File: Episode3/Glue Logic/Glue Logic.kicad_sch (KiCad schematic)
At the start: 5 parts, among them J1 5V DC

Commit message: Pushing back everything, due to PC reinstall.
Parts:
- removed A1: Arduino Mega 2560 R3, symbol 6309 v2.0:Arduino_Mega2560_R3_Shield
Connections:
- no-connect marks 38 -> 12
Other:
- sheet Logic Devices renamed Glue Logic
- sheet CPU, Reset & Buffers ports: added none; removed ~{RST_{trigger}}
- sheet Glue Logic: file PLD.kicad_sch -> Glue.kicad_sch
- sheet Glue Logic ports: added ~{CPU_{halt}}, ~{MRDY}, ~{RD}, ~{WR}; removed CLK_{in}, FW_{update}, RTC_{as}, RTC_{ds}, SPD_{led}^{G}, SPD_{led}^{R}, ~{ACIA1_{cs}}, ~{ACIA2_{cs}}, ~{CART_{cs}}, ~{CART_{detect}}, ~{CONST}, ~{FIRQ_{reg}}, ~{HALT_{bus}}, ~{HALT}, ~{IRQ_{reg}}, ~{RTC_{cs}}, ~{STAT_{reg}}, ~{UB_RD}, ~{UB_WR}

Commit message: Tied up a few loose ends in the PLD page.
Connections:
- no-connect marks 12 -> 38
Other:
- sheet Glue Logic ports: added PSG_{clk}, RTC_{as}, RTC_{ds}, SPD_{led}^{R}, WS[0..2], ~{ACIA_{cs}}, ~{CF_{cs}}, ~{CONST}, ~{FIRQ_{vec}}, ~{IRQ_{vec}}, ~{PAGE}, ~{PHY1_{reg}}, ~{PHY2_{reg}}, ~{PSG_{dtack}}, ~{REG}, ~{RTC_{cs}}, ~{STAT1_{reg}}, ~{STAT2_{reg}}, ~{TBC1}, ~{TBC2}, ~{TIMER_{cs}}, ~{VDP_{wait}}, ~{WAIT1}, ~{WAIT2}, ~{WAIT3}; removed none

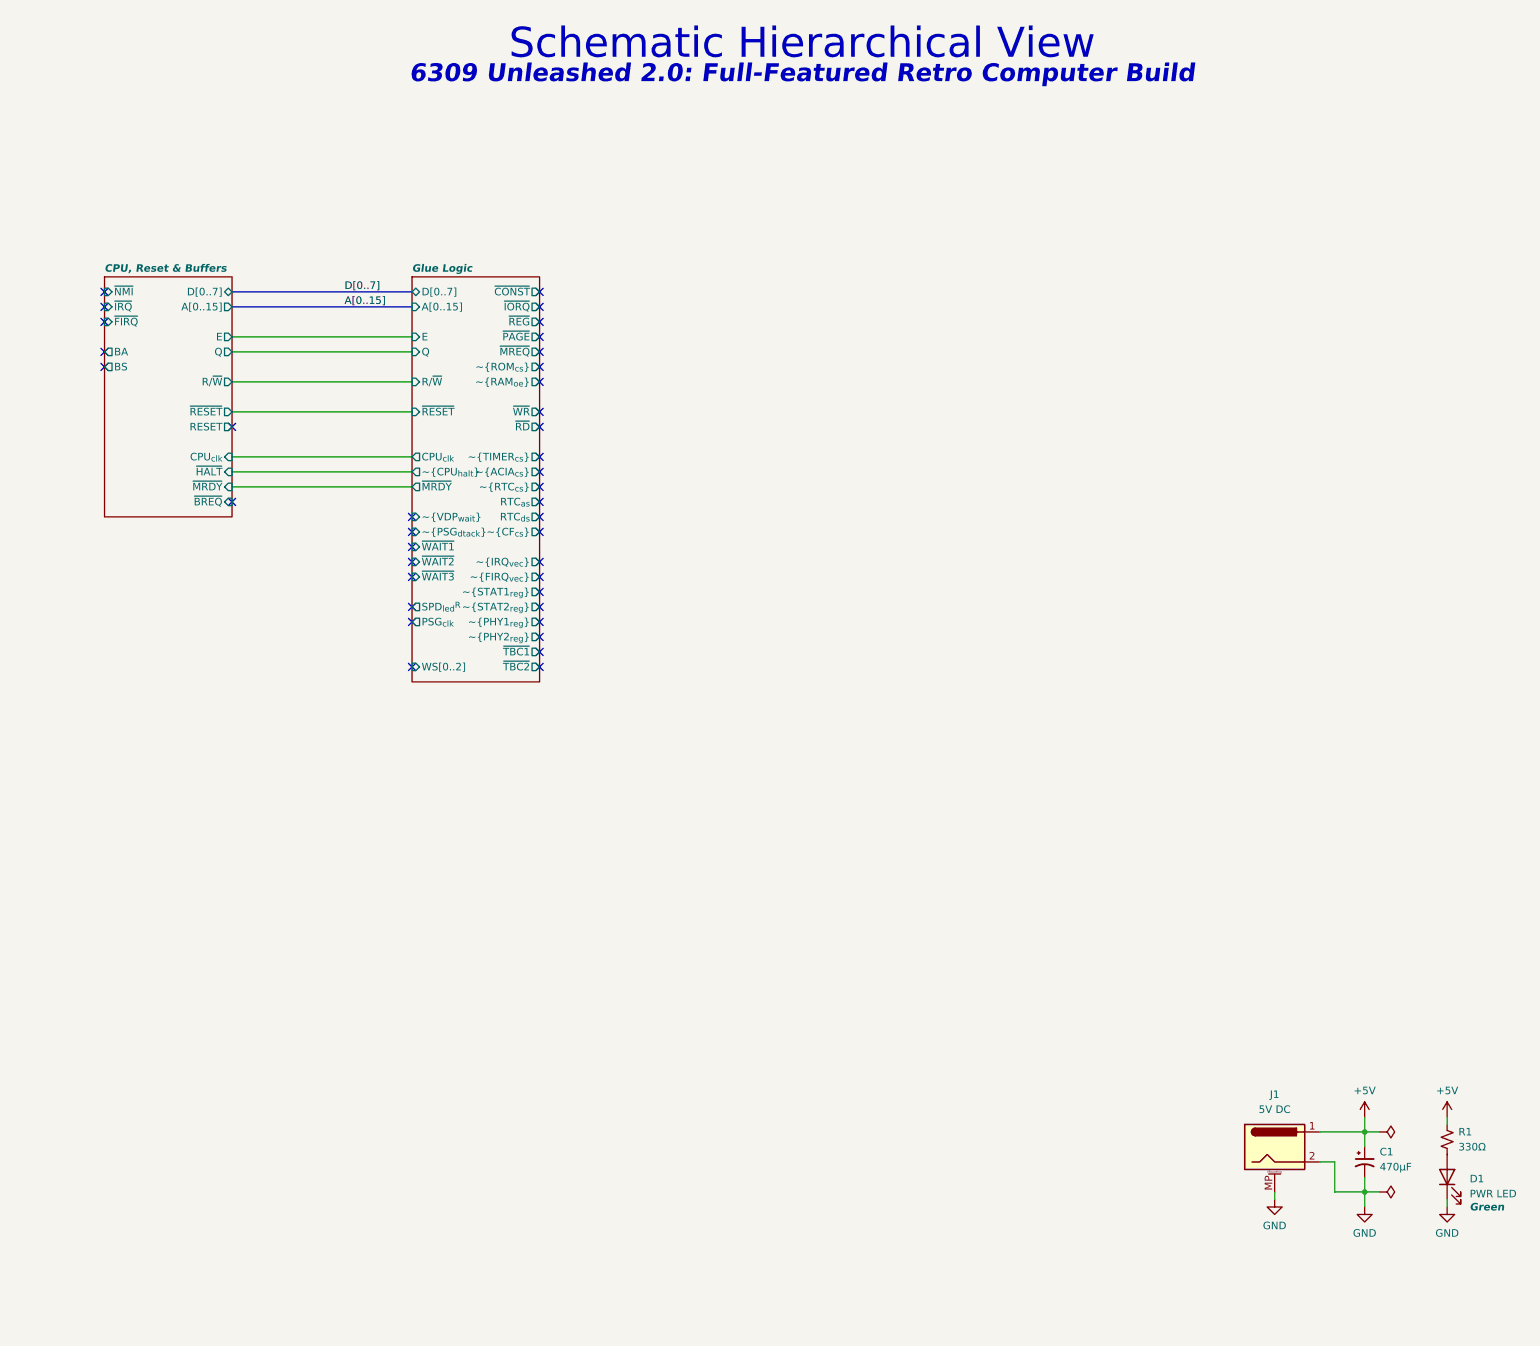
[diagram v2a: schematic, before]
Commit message: Reduced PLDs from 5 to 4, and optimized macrocells to the maximum
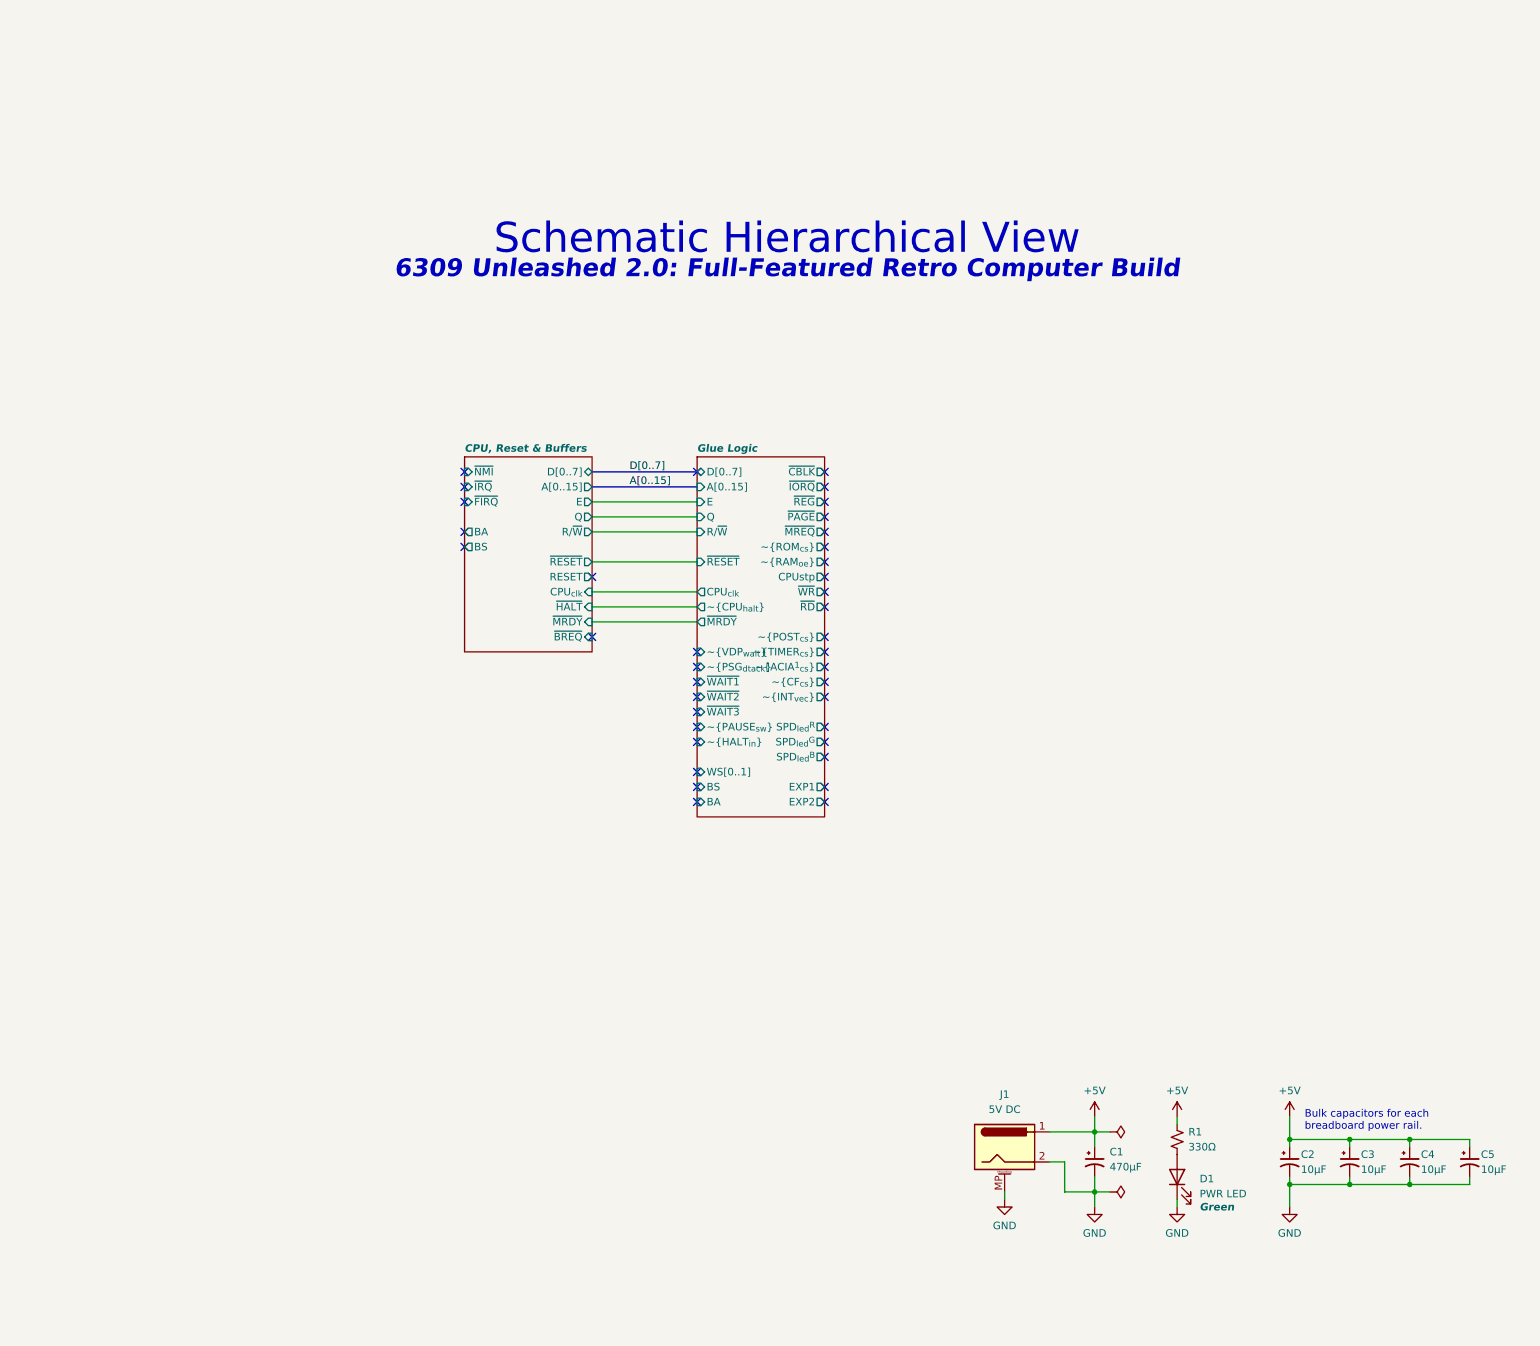
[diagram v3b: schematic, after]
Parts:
- added C2, C3, C4, C5: 10µF, symbol Device:C_Polarized_Small_US
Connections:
- net +5V: now also C2.1, C3.1, C4.1, C5.1
- net GND: now also C2.2, C3.2, C4.2, C5.2
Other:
- sheet Glue Logic ports: added BA, BS, CPUstp, EXP1, EXP2, SPD_{led}^{B}, SPD_{led}^{G}, WS[0..1], ~{ACIA^{1}_{cs}}, ~{CBLK}, ~{HALT_{in}}, ~{INT_{vec}}, ~{PAUSE_{sw}}, ~{POST_{cs}}; removed PSG_{clk}, RTC_{as}, RTC_{ds}, WS[0..2], ~{ACIA_{cs}}, ~{CONST}, ~{FIRQ_{vec}}, ~{IRQ_{vec}}, ~{PHY1_{reg}}, ~{PHY2_{reg}}, ~{RTC_{cs}}, ~{STAT1_{reg}}, ~{STAT2_{reg}}, ~{TBC1}, ~{TBC2}
- note added: "Bulk capacitors for each breadboard power rail."
- moved on the sheet: C1, D1, J1, R1

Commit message: Exploited every last macrocells I could.
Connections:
- no-connect marks 38 -> 32
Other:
- sheet Glue Logic ports: added none; removed EXP1, EXP2
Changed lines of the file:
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@@
+	)
+	(no_connect
+		(at 151.13 58.42)
+	)
+	(no_connect
+		(at 151.13 88.9)
+	)
+	(no_connect
+		(at 151.13 96.52)
+	)
+	(no_connect
+		(at 151.13 73.66)
+	)
+	(no_connect
+		(at 129.54 109.22)
+	)
+	(no_connect
+		(at 151.13 68.58)
+	)
+	(no_connect
+		(at 129.54 96.52)
+	)
+	(no_connect
+		(at 90.17 68.58)
+	)
+	(no_connect
+		(at 151.13 104.14)
+	)
+	(no_connect
+		(at 151.13 71.12)
+	)
+	(no_connect
+		(at 151.13 66.04)
+	)
+	(no_connect
+		(at 111.76 76.2)
+	)
+	(no_connect
+		(at 151.13 101.6)
+	)
+	(no_connect
+		(at 151.13 63.5)
+	)
+	(no_connect
+		(at 151.13 60.96)
+	)
+	(no_connect
+		(at 90.17 63.5)
+	)
+	(no_connect
+		(at 129.54 99.06)
+	)
+	(no_connect
+		(at 151.13 81.28)
 	)
 	(no_connect
@@
 	)
 	(no_connect
-		(at 151.13 58.42)
-	)
-	(no_connect
-		(at 151.13 88.9)
-	)
-	(no_connect
-		(at 90.17 71.12)
-	)
-	(no_connect
-		(at 151.13 96.52)
-	)
-	(no_connect
-		(at 151.13 73.66)
+		(at 129.54 58.42)
+	)
+	(no_connect
+		(at 151.13 93.98)
 	)
 	(no_connect
@@
 	)
 	(no_connect
-		(at 151.13 68.58)
-	)
-	(no_connect
-		(at 129.54 88.9)
-	)
-	(no_connect
-		(at 111.76 86.36)
-	)
-	(no_connect
-		(at 151.13 104.14)
-	)
-	(no_connect
-		(at 90.17 68.58)
-	)
-	(no_connect
-		(at 151.13 71.12)
-	)
-	(no_connect
-		(at 151.13 66.04)
-	)
-	(no_connect
-		(at 111.76 76.2)
-	)
-	(no_connect
-		(at 151.13 101.6)
-	)
-	(no_connect
-		(at 151.13 63.5)
-	)
-	(no_connect
-		(at 151.13 60.96)
-	)
-	(no_connect
-		(at 90.17 63.5)
-	)
-	(no_connect
-		(at 129.54 91.44)
-	)
-	(no_connect
-		(at 151.13 81.28)
+		(at 129.54 106.68)
+	)
+	(no_connect
+		(at 151.13 86.36)
+	)
+	(no_connect
+		(at 90.17 58.42)
+	)
+	(no_connect
+		(at 151.13 111.76)
+	)
+	(no_connect
+		(at 151.13 91.44)
+	)
+	(no_connect
+		(at 90.17 60.96)
+	)
+	(no_connect
+		(at 151.13 106.68)
 	)
 	(no_connect
@@
 	)
 	(no_connect
-		(at 129.54 58.42)
-	)
-	(no_connect
-		(at 151.13 93.98)
-	)
-	(no_connect
-		(at 129.54 93.98)
-	)
-	(no_connect
-		(at 129.54 99.06)
-	)
-	(no_connect
-		(at 151.13 86.36)
-	)
-	(no_connect
-		(at 90.17 58.42)
-	)
-	(no_connect
-		(at 151.13 91.44)
-	)
-	(no_connect
-		(at 129.54 114.3)
-	)
-	(no_connect
-		(at 90.17 60.96)
-	)
-	(no_connect
-		(at 151.13 114.3)
-	)
-	(no_connect
-		(at 129.54 109.22)
-	)
-	(no_connect
-		(at 151.13 106.68)
-	)
-	(no_connect
-		(at 129.54 96.52)
-	)
-	(no_connect
 		(at 151.13 78.74)
 	)
@@
 		(at 151.13 76.2)
 	)
-	(no_connect
-		(at 151.13 111.76)
-	)
 	(wire
 		(pts
@@
 	(wire
 		(pts
+			(xy 111.76 88.9) (xy 129.54 88.9)
+		)
+		(stroke
+			(width 0)
+			(type default)
+		)
+	)
+	(wire
+		(pts
 			(xy 181.61 181.61) (xy 181.61 180.34)
 		)
@@
 		(pts
 			(xy 229.87 167.64) (xy 229.87 171.45)
+		)
+		(stroke
+			(width 0)
+			(type default)
+		)
+	)
+	(wire
+		(pts
+			(xy 111.76 91.44) (xy 129.54 91.44)
 		)
 		(stroke
@@
 	(sheet
 		(at 90.17 55.88)
-		(size 21.59 33.02)
+		(size 21.59 38.1)
 		(exclude_from_sim no)
 		(in_bom yes)
@@
 		)
 		(property "Sheetfile" "CPU_RESET_BUFFERS.kicad_sch"
-			(at 90.17 89.4846 0)
+			(at 90.17 94.5646 0)
 			(effects
 				(font
@@
 		)
 		(pin "BS" output
-			(at 90.17 71.12 180)
-			(effects
-				(font
-					(size 1.27 1.27)
-				)
-				(justify left)
+			(at 111.76 91.44 0)
+			(effects
+				(font
+					(size 1.27 1.27)
+				)
+				(justify right)
 			)
 		)
@@
 		)
 		(pin "BA" output
-			(at 90.17 68.58 180)
-			(effects
-				(font
-					(size 1.27 1.27)
-				)
-				(justify left)
+			(at 111.76 88.9 0)
+			(effects
+				(font
+					(size 1.27 1.27)
+				)
+				(justify right)
 			)
 		)
@@
 		)
 		(pin "~{BREQ}" input
-			(at 111.76 86.36 0)
-			(effects
-				(font
-					(size 1.27 1.27)
-				)
-				(justify right)
+			(at 90.17 68.58 180)
+			(effects
+				(font
+					(size 1.27 1.27)
+				)
+				(justify left)
 			)
 		)
@@
 	(sheet
 		(at 129.54 55.88)
-		(size 21.59 60.96)
+		(size 21.59 58.42)
 		(exclude_from_sim no)
 		(in_bom yes)
@@
 		)
 		(property "Sheetfile" "Glue.kicad_sch"
-			(at 129.54 117.4246 0)
+			(at 129.54 114.8846 0)
 			(effects
 				(font
@@
 		)
 		(pin "~{PSG_{dtack}}" input
-			(at 129.54 91.44 180)
+			(at 129.54 99.06 180)
 			(effects
 				(font
@@
 		)
 		(pin "WS[0..1]" input
-			(at 129.54 109.22 180)
-			(effects
-				(font
-					(size 1.27 1.27)
-				)
-				(justify left)
+			(at 151.13 111.76 0)
+			(effects
+				(font
+					(size 1.27 1.27)
+				)
+				(justify right)
 			)
 		)
@@
 		)
 		(pin "~{WAIT1}" input
-			(at 129.54 93.98 180)
+			(at 129.54 101.6 180)
 			(effects
 				(font
@@
 		)
 		(pin "~{WAIT2}" input
+			(at 129.54 104.14 180)
+			(effects
+				(font
+					(size 1.27 1.27)
+				)
+				(justify left)
+			)
+		)
+		(pin "~{VDP_{wait}}" input
 			(at 129.54 96.52 180)
 			(effects
@@
 			)
 		)
-		(pin "~{VDP_{wait}}" input
-			(at 129.54 88.9 180)
-			(effects
-				(font
-					(size 1.27 1.27)
-				)
-				(justify left)
-			)
-		)
 		(pin "~{WAIT3}" input
-			(at 129.54 99.06 180)
+			(at 129.54 106.68 180)
 			(effects
 				(font
@@
 		)
 		(pin "~{PAUSE_{sw}}" input
-			(at 129.54 101.6 180)
+			(at 129.54 109.22 180)
 			(effects
 				(font
@@
 		)
 		(pin "~{HALT_{in}}" input
-			(at 129.54 104.14 180)
+			(at 129.54 111.76 180)
 			(effects
 				(font
@@
 		)
 		(pin "BA" input
-			(at 129.54 114.3 180)
+			(at 129.54 88.9 180)
 			(effects
 				(font
@@
 		)
 		(pin "BS" input
-			(at 129.54 111.76 180)
+			(at 129.54 91.44 180)
 			(effects
 				(font
@@
 			(effects
 				(font
-					(size 1.27 1.27)
-				)
-				(justify right)
-			)
-		)
-		(pin "EXP2" output
-			(at 151.13 114.3 0)
-			(effects
-				(font
-					(size 1.27 1.27)
-				)
-				(justify right)
-			)
-		)
-		(pin "EXP1" output
-			(at 151.13 111.76 0)
-			(effects
-				(font
